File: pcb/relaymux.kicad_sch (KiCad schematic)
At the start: 60 parts, among them J1 A, J10 B4, J11 USB_C, J12 Debug, J2 A1, J3 A2, J4 A3, J5 A4, J6 B, J7 B1, J8 B2, J9 B3, K1 TQ2SA-5V, K2 TQ2SA-5V, K3 TQ2SA-5V, K4 TQ2SA-5V, K5 TQ2SA-5V, K6 TQ2SA-5V, K7 TQ2SA-5V, K8 TQ2SA-5V, SW1 Cycle, SW2 Boot/Clear, U1 STM32F042F4Px, U2 TBD62783A, U3 TPS2552D, U4 TLV70033_SOT23-5

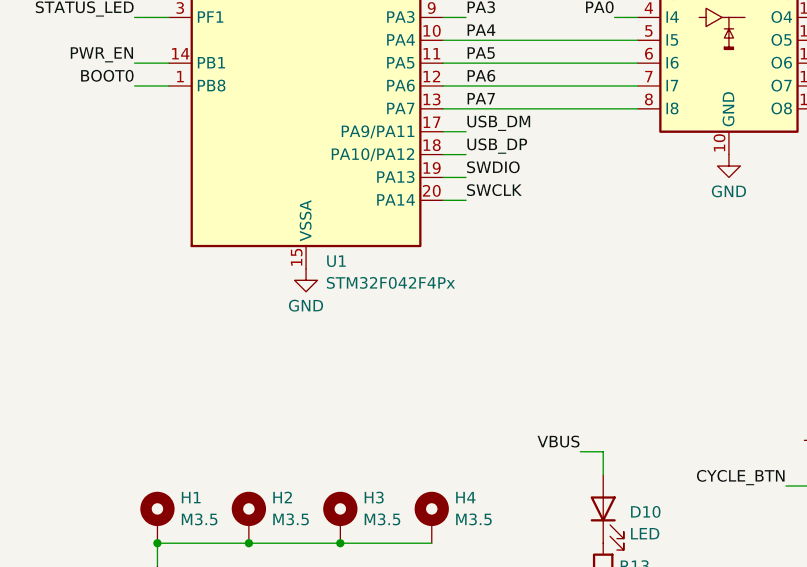
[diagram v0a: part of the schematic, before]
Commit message: Reorganize directories
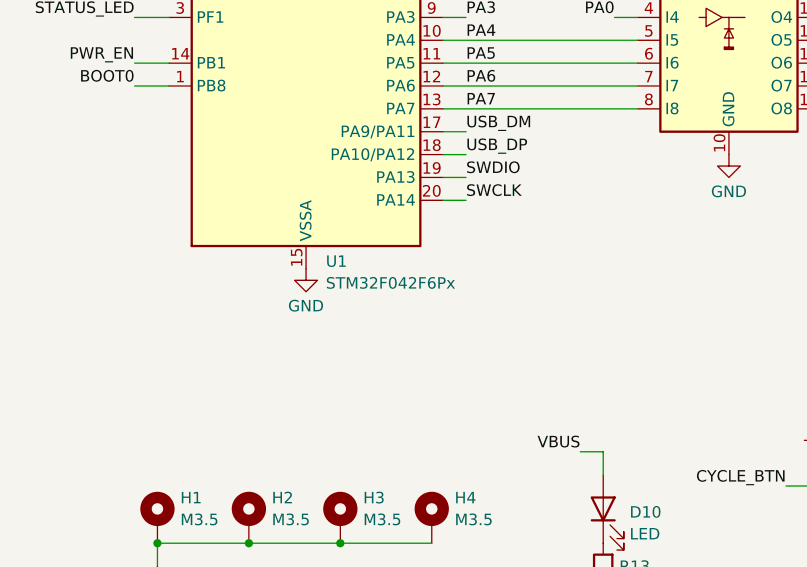
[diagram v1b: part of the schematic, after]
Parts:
- D1, D10, D2, D3, D4, D5, D6, D7, D8: MPN (none) -> LTST-C230KGKT
- K1, K2, K3, K4, K5, K6, K7, K8: MPN (none) -> TQ2SA-5V
- U1: value STM32F042F4Px -> STM32F042F6Px

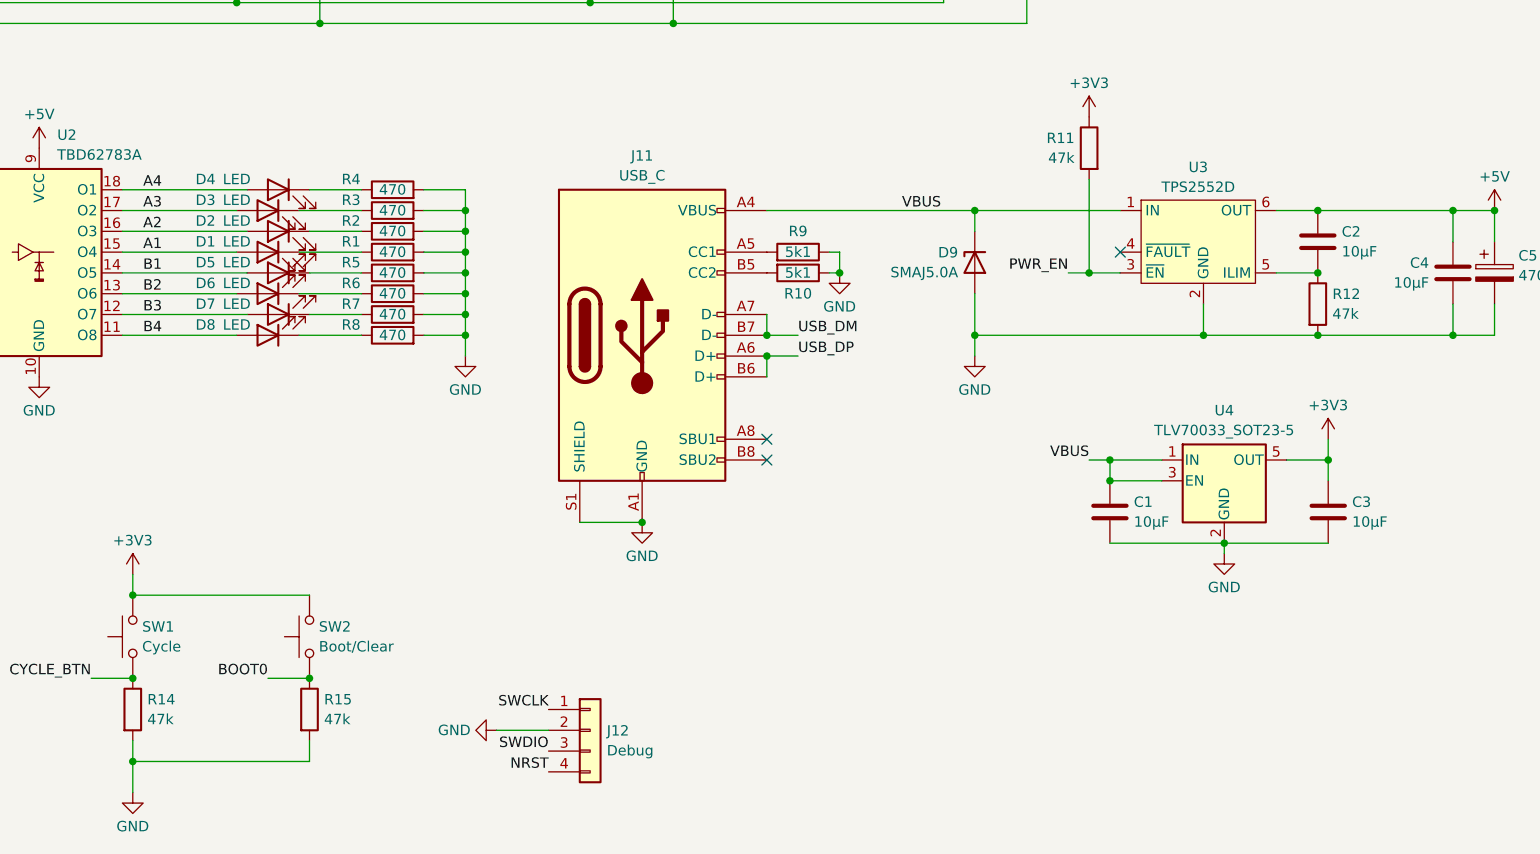
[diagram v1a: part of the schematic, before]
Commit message: First version of firmware
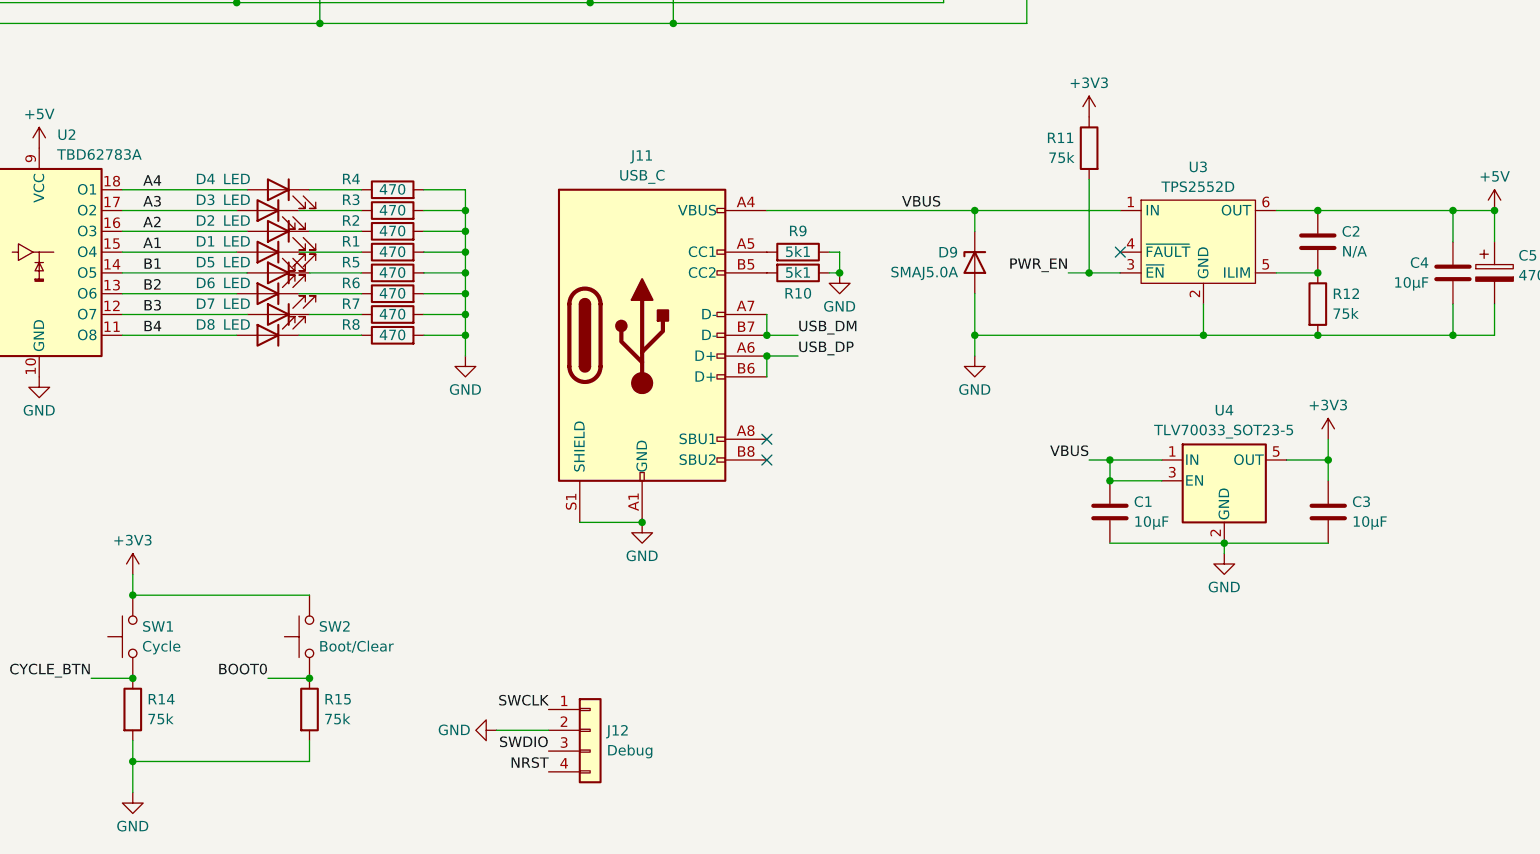
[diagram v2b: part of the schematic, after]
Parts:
- C2: value 10µF -> N/A
- R11, R12, R14, R15: value 47k -> 75k
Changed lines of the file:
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@@
       (effects (font (size 1.27 1.27)) (justify left))
     )
-    (property "Value" "10µF" (at 253.111 116.7821 0)
+    (property "Value" "N/A" (at 253.111 116.7821 0)
       (effects (font (size 1.27 1.27)) (justify left))
     )
@@
       (effects (font (size 1.27 1.27)) (justify left))
     )
-    (property "Value" "47k" (at 251.968 124.4021 0)
+    (property "Value" "75k" (at 251.968 124.4021 0)
       (effects (font (size 1.27 1.27)) (justify left))
     )
@@
       (effects (font (size 1.27 1.27)) (justify left))
     )
-    (property "Value" "47k" (at 128.778 173.9321 0)
+    (property "Value" "75k" (at 128.778 173.9321 0)
       (effects (font (size 1.27 1.27)) (justify left))
     )
@@
       (effects (font (size 1.27 1.27)) (justify left))
     )
-    (property "Value" "47k" (at 107.188 173.9321 0)
+    (property "Value" "75k" (at 107.188 173.9321 0)
       (effects (font (size 1.27 1.27)) (justify left))
     )
@@
       (effects (font (size 1.27 1.27)) (justify left))
     )
-    (property "Value" "47k" (at 220.472 105.3521 0)
-      (effects (font (size 1.27 1.27)) (justify left))
-    )
+    (property "Value" "75k" (at 220.472 105.3521 0)
+      (effects (font (size 1.27 1.27)) (justify left))
+    )

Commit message: Add readme, BOM
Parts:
- removed C2: N/A, Capacitor_SMD:C_0805_2012Metric, symbol Device:C
- C1, C3, C4: LCSC (none) -> C15850; MPN (none) -> CL21A106KAYNNNE
- C5: LCSC (none) -> C251022; MPN (none) -> UWD1E471MCL1GS
- D1, D10, D2, D3, D4, D5, D6, D7, D8: LCSC (none) -> C125106
- D9: LCSC (none) -> C2925443; MPN (none) -> SMAJ5.0A
- J11: footprint Connector_USB:USB_C_Receptacle_JAE_DX07S016JA1R1500 -> Connector_USB:USB_C_Receptacle_XKB_U262-16XN-4BVC11; LCSC (none) -> C319148; MPN (none) -> USB4110
- K1, K2, K3, K4, K5, K6, K7, K8: LCSC (none) -> C2858038
- R1, R13, R2, R3, R4, R5, R6, R7, R8: LCSC (none) -> C17710; MPN (none) -> Generic 470 ohm 0805
- R10, R9: LCSC (none) -> C27834; MPN (none) -> Generic 5.1kohm 0805
- R11, R12, R14, R15: value 75k -> 68k; LCSC (none) -> C17801; MPN (none) -> Generic 68kohm 0805
- SW1, SW2: LCSC (none) -> C273375; MPN (none) -> 320E11BLK
- U1: LCSC (none) -> C2969989; MPN (none) -> STM32F042F6P6
- U2: LCSC (none) -> C97745; MPN (none) -> TBD62783AFG,EL
- U3: LCSC (none) -> C46506; MPN (none) -> TPS2552DBVR
- U4: LCSC (none) -> C11337; MPN (none) -> TLV70033DDCR
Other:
- note added: "TBD62783A has integrated flyback diodes and input pulldown resistors."
- note added: "U3 acts as inrush current limiter, limit is set at 350 mA."
- moved on the sheet: D5, D6, D7, D8
